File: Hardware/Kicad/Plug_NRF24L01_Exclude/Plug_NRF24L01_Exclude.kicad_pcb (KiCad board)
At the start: 2 copper layers, 36 x 30 mm, 38 parts, among them J1 Conn_02x07_Odd_Even, J2 Conn_01x08_Socket, J3 Conn_01x07_Socket, Q1 2N7002, Q2 2N7002, Q3 2N7002, Q4 2N7002, Q5 2N7002, SW1 SW_SPST, U1 STM32L412KBTx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

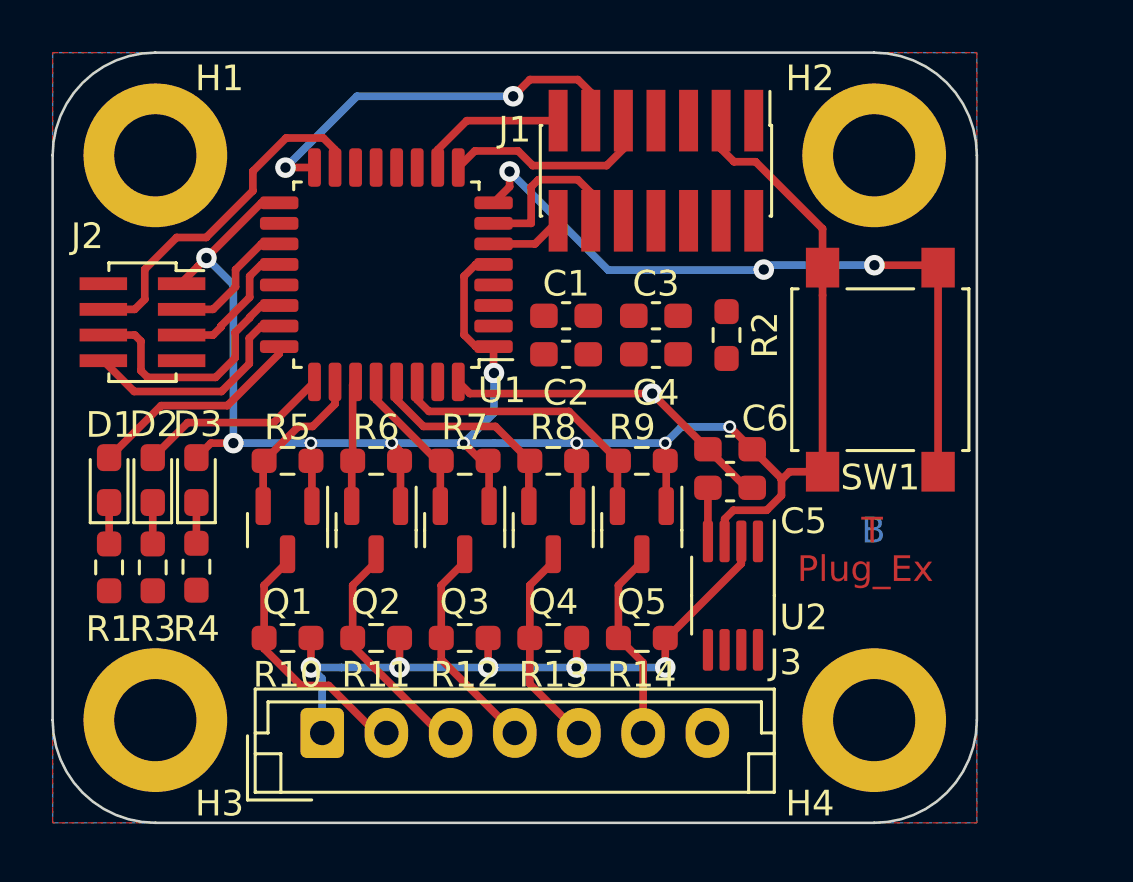
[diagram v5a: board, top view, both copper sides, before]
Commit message: Updated Plug_NRF24L01_Exclude (V2.0) - Schematic (NRF24 Connector) - PCB (Capacitor)
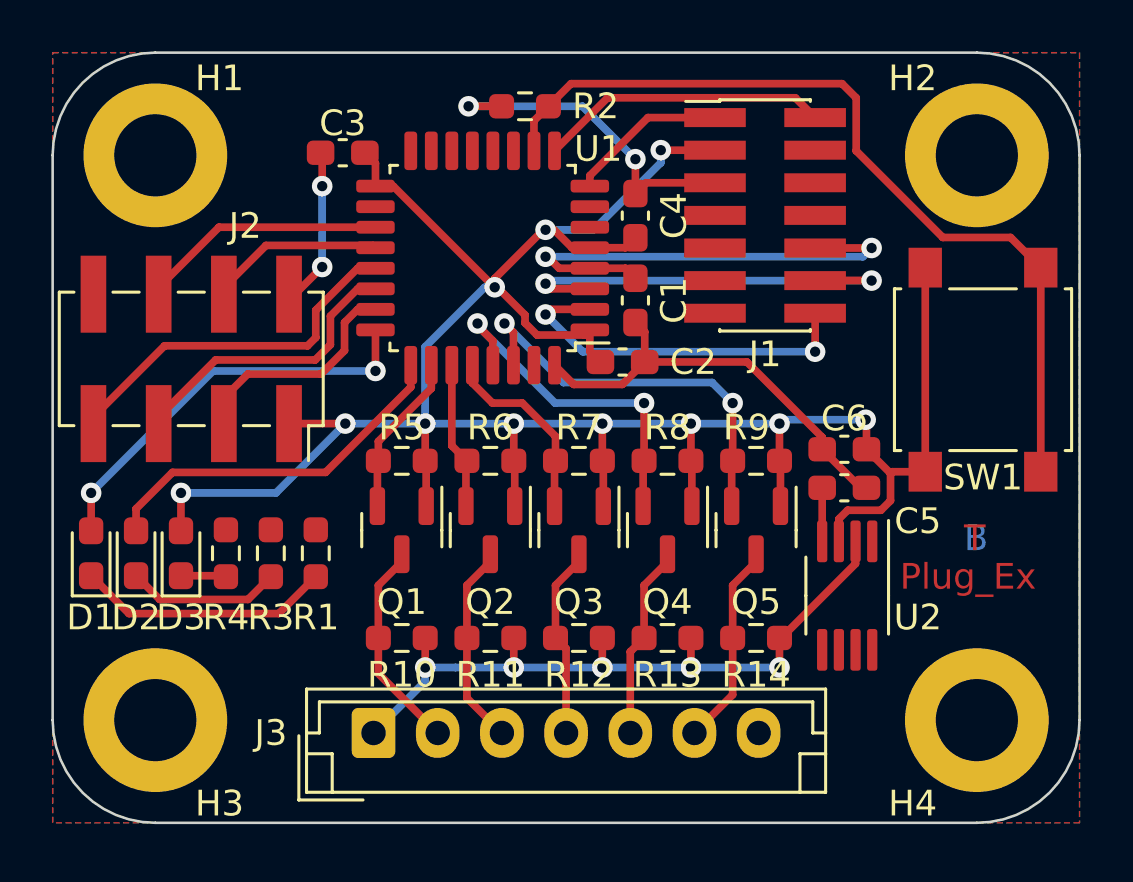
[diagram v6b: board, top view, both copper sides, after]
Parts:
- J2: footprint Connector_PinSocket_1.00mm:PinSocket_2x04_P1.00mm_Vertical_SMD -> Connector_PinSocket_2.54mm:PinSocket_2x04_P2.54mm_Vertical_SMD
- moved C3 13.8 mm to (109.3, 77.9), turned to 180 degrees
- moved R2 11.9 mm to (116.4, 76.1), turned to 180 degrees
- moved R1 8.07 mm to (108.2, 93.5), turned to 90 degrees
- moved C4 5.46 mm to (120.7, 80.3), turned to 90 degrees
- moved R3 4.63 mm to (106.5, 93.5), turned to 90 degrees
- moved J1 4.59 mm to (125.8, 80.3), turned to 0 degrees
- moved C5 4.45 mm to (128.8, 91.0)
- moved C6 4.45 mm to (128.8, 89.5)
- moved Q2 4.45 mm to (115.0, 92.6)
- moved Q3 4.45 mm to (118.5, 92.6)
- moved Q4 4.45 mm to (122.0, 92.6)
- moved Q5 4.45 mm to (125.4, 92.6)
- moved R11 4.45 mm to (115.0, 96.8)
- moved R12 4.45 mm to (118.5, 96.8)
- moved R13 4.45 mm to (122.0, 96.8)
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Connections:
- J1 pad 1: unconnected-(J1-Pin_1-Pad1) -> SWDCK
- J1 pad 13: SWDCK -> unconnected-(J1-Pin_13-Pad13)
- J1 pad 2: unconnected-(J1-Pin_2-Pad2) -> SWDIO
- J1 pad 9: SWDIO -> unconnected-(J1-Pin_9-Pad9)
- J2 pad 3: SPI_Chip_Select -> Chip_Enable
- J2 pad 4: Chip_Enable -> SPI_Digital_Input
- J2 pad 5: SPI_Digital_Input -> SPI_Clock
- J2 pad 6: SPI_Clock -> SPI_Digital_Output
- J2 pad 7: unconnected-(J2-Pin_7-Pad7) -> SPI_Chip_Select
- J2 pad 8: SPI_Digital_Output -> unconnected-(J2-Pin_8-Pad8)
- U1 pad 10: SWDCK -> Appairing_Btn
- U1 pad 15: Chip_Enable -> unconnected-(U1-PB1-Pad15)
- U1 pad 19: SPI_Chip_Select -> SPI_Digital_Output
- U1 pad 2: unconnected-(U1-PC14-Pad2) -> USART2_TX
- U1 pad 21: unconnected-(U1-PA11-Pad21) -> SPI_Chip_Select
- U1 pad 23: SPI_Digital_Output -> Chip_Enable
- U1 pad 3: unconnected-(U1-PC15-Pad3) -> USART2_RX
- U1 pad 6: USART2_TX -> unconnected-(U1-PA0-Pad6)
- U1 pad 7: USART2_RX -> unconnected-(U1-PA1-Pad7)
- U1 pad 8: Appairing_Btn -> SWDCK
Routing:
- net NRST: track 0.00 -> 18.9 mm, vias 0 -> 2
- net +3.3V: track 82.5 -> 99.5 mm, vias 9 -> 11
- net USART2_TX: track 2.89 -> 14.4 mm, vias 0 -> 2
- net USART2_RX: track 6.63 -> 16.8 mm, vias 0 -> 2
- net SPI_Chip_Select: track 5.25 -> 14.5 mm
- net Net-(D1-K): track 1.61 -> 9.96 mm
- net Player1_LED: track 8.58 -> 16.1 mm, vias 0 -> 2
- net GND: track 28.9 -> 36.3 mm, vias 3 -> 4
- net Status_LED: track 7.52 -> 14.4 mm
- net Appairing_Btn: track 27.8 -> 33.6 mm, vias 3 -> 0
- net Serial_Data2_STM32: track 8.64 -> 13.7 mm, vias 0 -> 2
- net Chip_Enable: track 13.8 -> 8.97 mm
- net IOBit_STM32: track 11.3 -> 16.0 mm, vias 0 -> 2
- net Net-(D2-K): track 1.61 -> 6.00 mm
- net SWDIO: track 8.30 -> 11.3 mm
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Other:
- board size 36 x 30 mm -> 40 x 30 mm

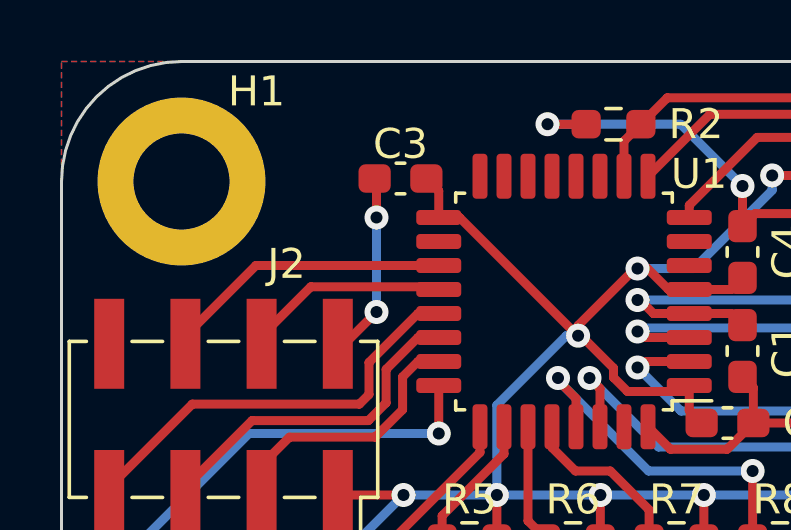
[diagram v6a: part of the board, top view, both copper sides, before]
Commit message: Updated Plug_NRF24L01_Exclude (V2.1) - Schematic & PCB (Added 10μ Capacitor)
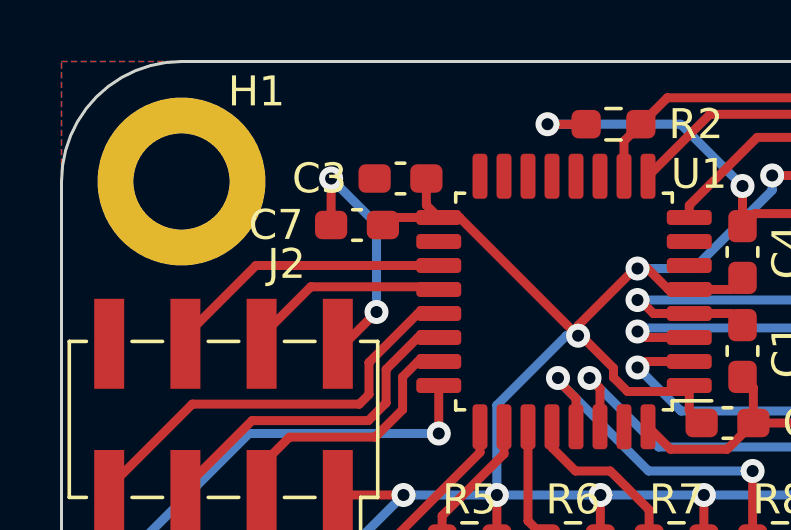
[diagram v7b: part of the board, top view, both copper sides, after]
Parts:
- added C7: 10u, Capacitor_SMD:C_0603_1608Metric_Pad1.08x0.95mm_HandSolder, F.Cu at (107.8, 79.5)
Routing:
- net GND: track 36.3 -> 38.7 mm
- net +3.3V: track 99.5 -> 101.4 mm

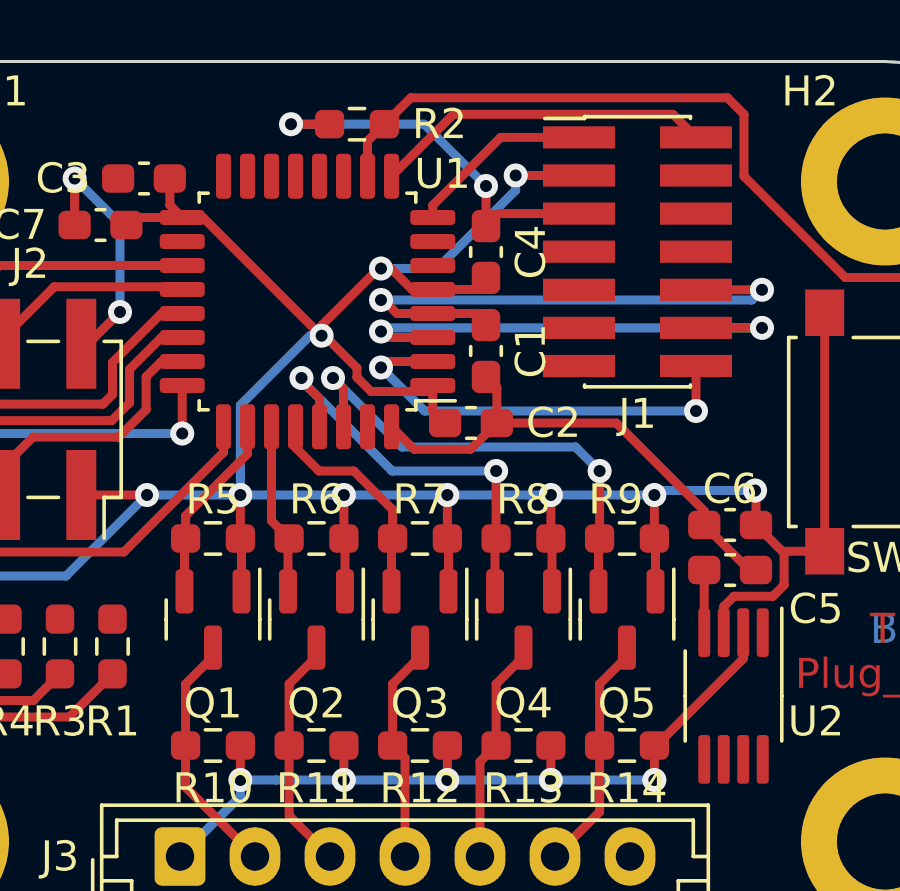
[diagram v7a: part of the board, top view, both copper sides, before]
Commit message: Updated Plug_NRF24L01_Exclude (Ground vias)
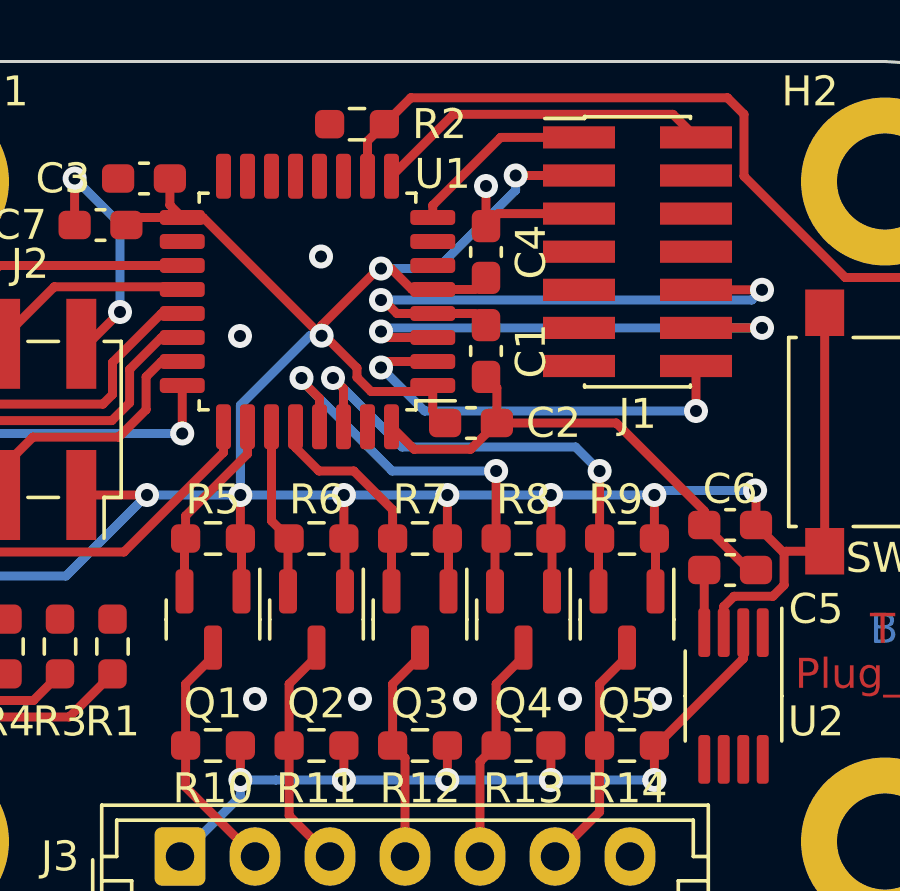
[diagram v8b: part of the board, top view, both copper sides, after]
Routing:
- net GND: track 38.7 -> 30.0 mm, vias 4 -> 10
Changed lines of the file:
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@@
   (segment (start 122.8625 97.95) (end 126.3125 97.95) (width 0.3) (layer "B.Cu") (net 1))
   (segment (start 120.7 79.4875) (end 120.7 78.15) (width 0.3) (layer "F.Cu") (net 2))
-  (segment (start 114.2 76.09) (end 115.4875 76.09) (width 0.3) (layer "F.Cu") (net 2))
   (segment (start 127.975 89.45) (end 127.975 88.981129) (width 0.3) (layer "F.Cu") (net 2))
   (segment (start 127.975 88.981129) (end 125.043871 86.05) (width 0.3) (layer "F.Cu") (net 2))
@@
   (segment (start 106.9875 77.9375) (end 106.9 77.85) (width 0.3) (layer "F.Cu") (net 2))
   (segment (start 121.0625 86.05) (end 121.0625 84.875) (width 0.3) (layer "F.Cu") (net 2))
-  (via (at 114.2 76.09) (size 0.8) (drill 0.4) (layers "F.Cu" "B.Cu") (net 2))
+  (via (at 116.5 95.25) (size 0.8) (drill 0.4) (layers "F.Cu" "B.Cu") (free) (net 2))
+  (via (at 112.5 83.15) (size 0.8) (drill 0.4) (layers "F.Cu" "B.Cu") (free) (net 2))
+  (via (at 113 95.25) (size 0.8) (drill 0.4) (layers "F.Cu" "B.Cu") (free) (net 2))
+  (via (at 115.2 80.5) (size 0.8) (drill 0.4) (layers "F.Cu" "B.Cu") (free) (net 2))
   (via (at 108.5 82.35) (size 0.8) (drill 0.4) (layers "F.Cu" "B.Cu") (net 2))
   (via (at 106.9875 77.9) (size 0.8) (drill 0.4) (layers "F.Cu" "B.Cu") (net 2))
+  (via (at 123.5 95.25) (size 0.8) (drill 0.4) (layers "F.Cu" "B.Cu") (free) (net 2))
+  (via (at 126.5 95.25) (size 0.8) (drill 0.4) (layers "F.Cu" "B.Cu") (free) (net 2))
   (via (at 120.7 78.15) (size 0.8) (drill 0.4) (layers "F.Cu" "B.Cu") (net 2))
+  (via (at 120 95.25) (size 0.8) (drill 0.4) (layers "F.Cu" "B.Cu") (free) (net 2))
   (segment (start 108.5 79.4125) (end 106.9875 77.9) (width 0.3) (layer "B.Cu") (net 2))
-  (segment (start 120.7 78.15) (end 118.64 76.09) (width 0.3) (layer "B.Cu") (net 2))
-  (segment (start 118.64 76.09) (end 114.2 76.09) (width 0.3) (layer "B.Cu") (net 2))
   (segment (start 108.5 82.35) (end 108.5 79.4125) (width 0.3) (layer "B.Cu") (net 2))
   (segment (start 128.967893 91.825) (end 130.264061 91.825) (width 0.3) (layer "F.Cu") (net 3))
